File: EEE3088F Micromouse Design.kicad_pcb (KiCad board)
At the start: 2 copper layers, 70 x 78.2 mm, 47 parts, among them J1 Conn_02x16_Odd_Even, J2 Conn_01x02, J3 TYPE-C-31-M-12, SW1 SW_SPDT, U1 INA219AxD, U2 XL1509-3.3, U7 TPS61088RHLR, U9 CH224K

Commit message: Added a bunch of changes
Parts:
- removed C2, C4, C5, C6: 100uF, Capacitor_SMD:C_1206_3216Metric_Pad1.33x1.80mm_HandSolder
- removed C7: 47uF, Capacitor_SMD:C_1206_3216Metric_Pad1.33x1.80mm_HandSolder
- removed D1: 1N5819, Diode_THT:D_DO-41_SOD81_P10.16mm_Horizontal
- added C12: 100uF, Capacitor_Tantalum_SMD:CP_EIA-3528-21_Kemet-B, F.Cu at (182.1, 121.7)
- added C14: 47uF, Capacitor_SMD:C_1206_3216Metric_Pad1.33x1.80mm_HandSolder, F.Cu at (182.1, 125.0)
- added C15: 47uF, Capacitor_SMD:C_1206_3216Metric_Pad1.33x1.80mm_HandSolder, F.Cu at (182.1, 128.4)
- added C26: 100uF, Capacitor_Tantalum_SMD:CP_EIA-3528-21_Kemet-B, F.Cu at (188.8, 114.0)
- added C27: 1uF, Capacitor_SMD:C_0402_1005Metric_Pad0.74x0.62mm_HandSolder, F.Cu at (182.9, 94.7)
- added C28: 10nF, Capacitor_SMD:C_0603_1608Metric, F.Cu at (175.9, 142.8)
- added C29: 2.2uF, Capacitor_SMD:C_0603_1608Metric_Pad1.08x0.95mm_HandSolder, F.Cu at (180.0, 139.1)
- added C30: 10nF, Capacitor_SMD:C_0603_1608Metric, F.Cu at (162.0, 145.8)
- added C31: 2.2uF, Capacitor_SMD:C_0603_1608Metric_Pad1.08x0.95mm_HandSolder, F.Cu at (153.8, 136.2)
- added C32: 1uF, Capacitor_SMD:C_0402_1005Metric_Pad0.74x0.62mm_HandSolder, F.Cu at (182.9, 96.7)
- added C33: 1uF, Capacitor_SMD:C_0402_1005Metric_Pad0.74x0.62mm_HandSolder, F.Cu at (182.9, 98.7)
- added C34: 1uF, Capacitor_SMD:C_0402_1005Metric_Pad0.74x0.62mm_HandSolder, F.Cu at (182.9, 100.6)
- added C35: 1nF, Capacitor_SMD:C_0603_1608Metric, F.Cu at (179.0, 97.5)
- added C36: 1nF, Capacitor_SMD:C_0603_1608Metric, F.Cu at (179.0, 100.0)
- added C37: 100uF, Capacitor_Tantalum_SMD:CP_EIA-3528-21_Kemet-B, F.Cu at (115.8, 101.5)
- added C38: 100uF, Capacitor_Tantalum_SMD:CP_EIA-3528-21_Kemet-B, F.Cu at (115.8, 105.9)
- added C40: 100uF, Capacitor_Tantalum_SMD:CP_EIA-3528-21_Kemet-B, F.Cu at (115.8, 110.2)
- added C41: 10uF, Capacitor_SMD:C_0805_2012Metric_Pad1.18x1.45mm_HandSolder, F.Cu at (180.1, 135.8)
- added C44: 10uF, Capacitor_SMD:C_0805_2012Metric_Pad1.18x1.45mm_HandSolder, F.Cu at (185.4, 91.9)
- added C45: 10uF, Capacitor_SMD:C_0805_2012Metric_Pad1.18x1.45mm_HandSolder, F.Cu at (162.4, 143.0)
- added C46: 100uF, Capacitor_Tantalum_SMD:CP_EIA-3528-21_Kemet-B, F.Cu at (115.8, 114.6)
- added C47: 47uF, Capacitor_SMD:C_1206_3216Metric_Pad1.33x1.80mm_HandSolder, F.Cu at (121.8, 105.6)
- added C48: 100uF, Capacitor_Tantalum_SMD:CP_EIA-3528-21_Kemet-B, F.Cu at (115.8, 118.9)
- added C49: 100uF, Capacitor_Tantalum_SMD:CP_EIA-3528-21_Kemet-B, F.Cu at (115.8, 123.3)
- added C50: 100uF, Capacitor_Tantalum_SMD:CP_EIA-3528-21_Kemet-B, F.Cu at (115.8, 127.6)
- added D3: SS32, Diode_SMD:D_SMA, F.Cu at (187.6, 117.3)
- added D4: SS32, Diode_SMD:D_SMA, F.Cu at (122.8, 101.6)
- added L3: 22uH, Inductor_SMD:L_7.3x7.3_H4.5, F.Cu at (204.4, 117.4)
- added L4: 22uH, Inductor_SMD:L_7.3x7.3_H4.5, F.Cu at (204.5, 125.7)
- added L5: 22uH, Inductor_SMD:L_7.3x7.3_H4.5, F.Cu at (204.7, 134.8)
- added Q2: AO3400A, Package_TO_SOT_SMD:SOT-23, F.Cu at (181.5, 113.6)
- added R19: 10k, Resistor_SMD:R_0603_1608Metric_Pad0.98x0.95mm_HandSolder, F.Cu at (179.1, 95.0)
- added R26: 1, Resistor_SMD:R_1206_3216Metric_Pad1.30x1.75mm_HandSolder, F.Cu at (180.2, 141.6)
- added R27: 4.7k, Resistor_SMD:R_1206_3216Metric_Pad1.30x1.75mm_HandSolder, F.Cu at (188.5, 121.8)
- added R28: 330, Resistor_SMD:R_0805_2012Metric_Pad1.20x1.40mm_HandSolder, F.Cu at (181.4, 117.3)
- added R29: 0.82, Resistor_SMD:R_0603_1608Metric_Pad0.98x0.95mm_HandSolder, F.Cu at (153.8, 138.7)
- added R30: 0.82, Resistor_SMD:R_0603_1608Metric_Pad0.98x0.95mm_HandSolder, F.Cu at (153.8, 141.2)
- added R31: 0.82, Resistor_SMD:R_0603_1608Metric_Pad0.98x0.95mm_HandSolder, F.Cu at (153.8, 143.7)
- added R32: 0.82, Resistor_SMD:R_0603_1608Metric_Pad0.98x0.95mm_HandSolder, F.Cu at (153.8, 146.2)
- added R33: 2.2k, Resistor_SMD:R_0603_1608Metric_Pad0.98x0.95mm_HandSolder, F.Cu at (187.7, 124.7)
- added R34: 270, Resistor_SMD:R_0603_1608Metric_Pad0.98x0.95mm_HandSolder, F.Cu at (187.7, 127.2)
- added R35: 1, Resistor_SMD:R_1206_3216Metric_Pad1.30x1.75mm_HandSolder, F.Cu at (171.6, 143.0)
- added TP10: TestPoint, TestPoint:TestPoint_Pad_D2.0mm, F.Cu at (171.2, 106.7)
- added TP11: TestPoint, TestPoint:TestPoint_Pad_D2.0mm, F.Cu at (171.2, 110.7)
- added TP12: TestPoint, TestPoint:TestPoint_Pad_D2.0mm, F.Cu at (171.2, 114.8)
- added TP13: TestPoint, TestPoint:TestPoint_Pad_D2.0mm, F.Cu at (171.2, 118.8)
- added TP14: TestPoint, TestPoint:TestPoint_Pad_D2.0mm, F.Cu at (171.2, 122.8)
- added TP2: TestPoint, TestPoint:TestPoint_Pad_D2.0mm, F.Cu at (180.1, 146.1)
- added TP4: TestPoint, TestPoint:TestPoint_Pad_D2.0mm, F.Cu at (173.9, 145.9)
- added TP6: TestPoint, TestPoint:TestPoint_Pad_D2.0mm, F.Cu at (158.0, 143.6)
- added TP8: TestPoint, TestPoint:TestPoint_Pad_D2.0mm, F.Cu at (158.0, 147.6)
- added U11: DRV8833PW, Package_SO:TSSOP-16_4.4x5mm_P0.65mm, F.Cu at (173.4, 137.6)
- added U12: DRV8833PW, Package_SO:TSSOP-16_4.4x5mm_P0.65mm, F.Cu at (160.7, 138.2)
- added U13: AP22966DC8-7, AP22966DC8-7:IC_AP22966DC8-7, F.Cu at (167.6, 99.1)
- added U14: XL1509-5.0, Package_SO:SOIC-8_3.9x4.9mm_P1.27mm, F.Cu at (195.8, 116.4)
- added U15: TP4056-42-ESOP8, Package_SO:SOIC-8-1EP_3.9x4.9mm_P1.27mm_EP2.41x3.3mm_ThermalVias, F.Cu at (195.8, 123.0)
- C13, C23, C25: footprint Capacitor_SMD:C_1206_3216Metric_Pad1.33x1.80mm_HandSolder -> Capacitor_Tantalum_SMD:CP_EIA-3528-21_Kemet-B
- moved C20 126.1 mm to (190.6, 95.8)
- moved C21 126.1 mm to (190.6, 99.1)
- moved C22 126.1 mm to (190.6, 102.5)
- moved TP20 126.1 mm to (207.7, 105.3)
- moved U7 126.1 mm to (202.3, 106.6)
- moved C1 126.1 mm to (204.2, 102.1)
- moved C16 126.1 mm to (189.2, 108.1)
- moved C17 126.1 mm to (189.2, 110.0)
- moved C18 126.1 mm to (201.8, 111.1)
- moved C19 126.1 mm to (195.6, 110.8)
- moved C39 126.1 mm to (200.8, 101.4)
- moved L2 126.1 mm to (201.8, 97.0)
- moved R21 126.1 mm to (196.6, 107.9)
- moved R4 126.1 mm to (196.0, 95.6)
- moved R5 126.1 mm to (196.6, 104.6)
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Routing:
- net GND: track 0.00 -> 17.1 mm
- net /MOTOR1_B_OUT: track 0.00 -> 3.52 mm
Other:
- board size 70 x 78.2 mm -> 70.2 x 78.6 mm
- board text added: "200mA Motor"
- board text added: "500mA Motor"
- board text added: "Battery Charging"
- board text added: "External Load Switching"

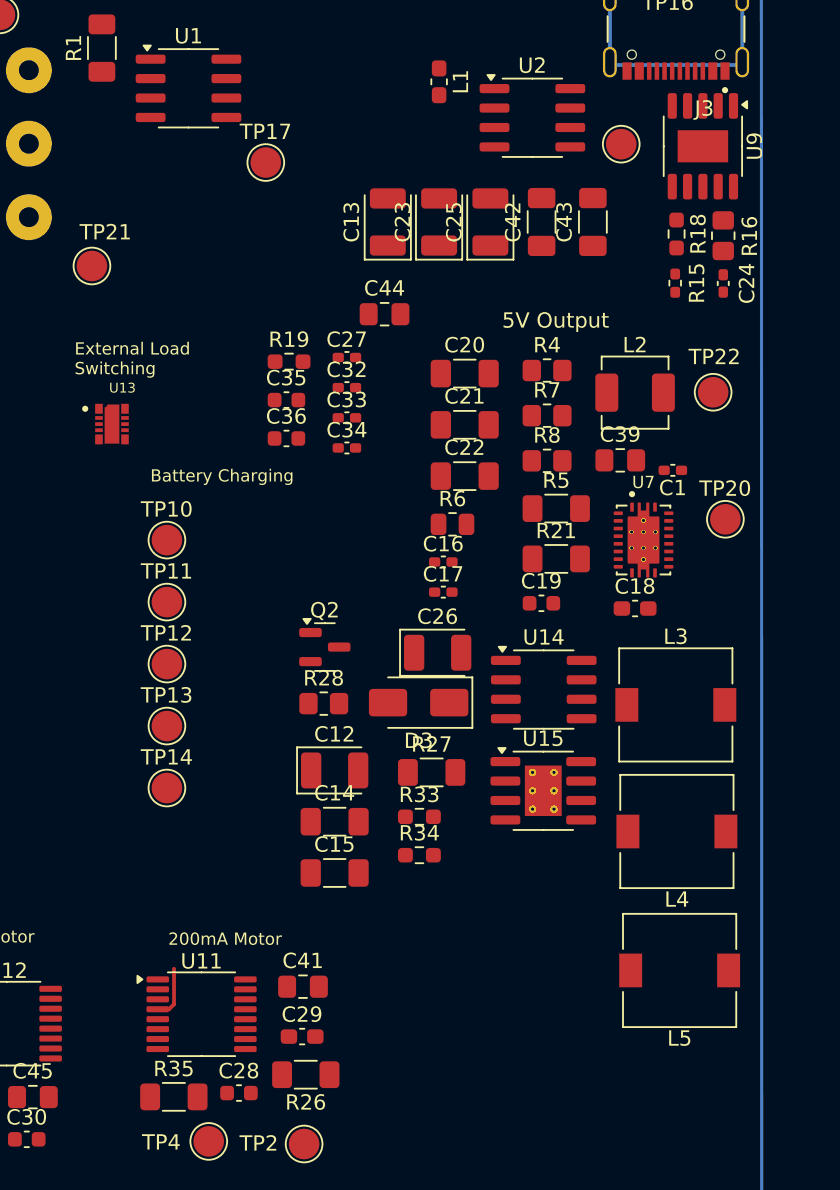
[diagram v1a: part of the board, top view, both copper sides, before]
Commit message: Updated the INA219 circuit
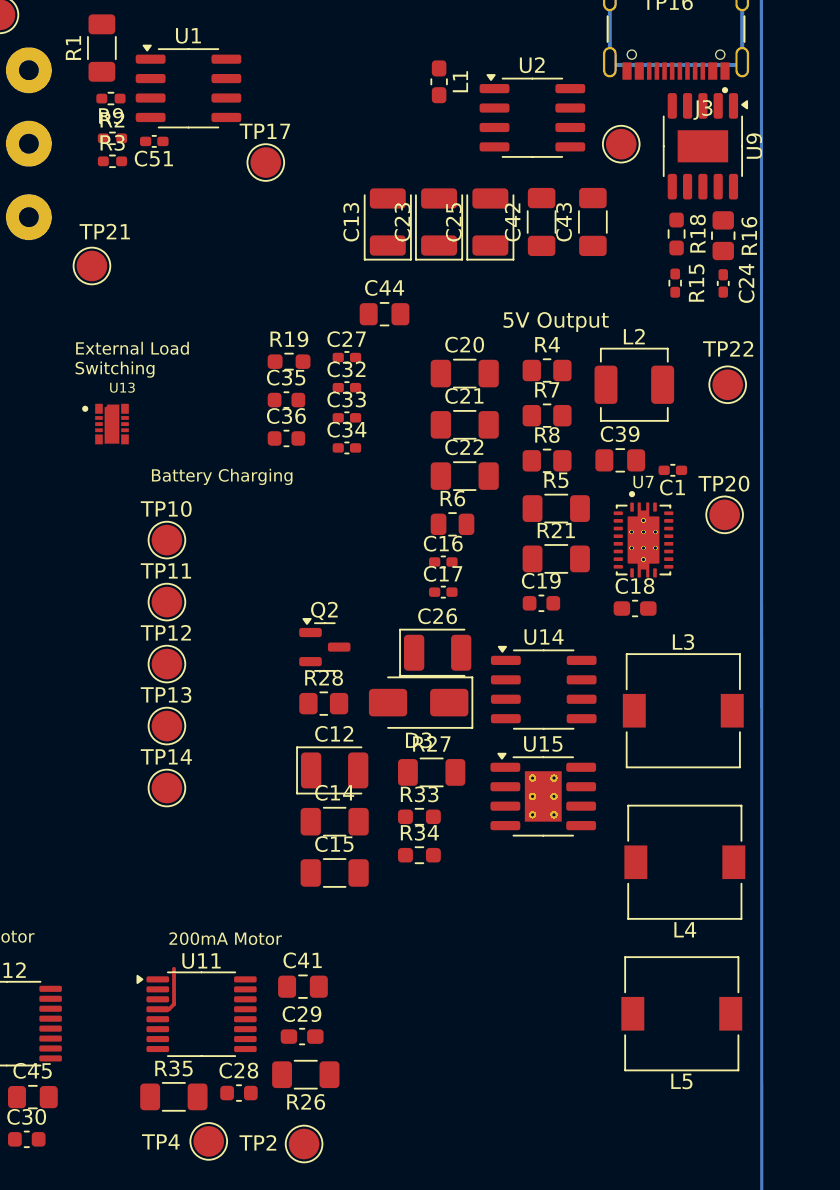
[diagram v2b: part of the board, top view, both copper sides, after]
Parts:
- added C51: 0.1uF, Capacitor_SMD:C_0402_1005Metric_Pad0.74x0.62mm_HandSolder, F.Cu at (170.3, 80.6)
- added R2: 3.3k, Resistor_SMD:R_0402_1005Metric_Pad0.72x0.64mm_HandSolder, F.Cu at (167.6, 80.4)
- added R3: 3.3k, Resistor_SMD:R_0402_1005Metric_Pad0.72x0.64mm_HandSolder, F.Cu at (167.6, 81.9)
- added R9: 3.3k, Resistor_SMD:R_0402_1005Metric_Pad0.72x0.64mm_HandSolder, F.Cu at (167.5, 77.8)
- moved L5 2.83 mm to (204.8, 137.6)
- moved L4 2.08 mm to (205.0, 127.7)
- moved TP22 1.07 mm to (207.8, 96.5)
- moved L3 0.62 mm to (204.9, 117.8)
- moved L2 0.52 mm to (201.7, 96.5)
- moved U15 0.37 mm to (195.8, 123.4)
- moved TP20 0.29 mm to (207.6, 105.0)
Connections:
- U1 pad 1: /V_Battery+ -> Net-(U1-A1)
- U1 pad 3: /SDA_INA219 -> Net-(U1-SDA)
- U1 pad 4: /SCLK_INA219 -> Net-(U1-SCL)

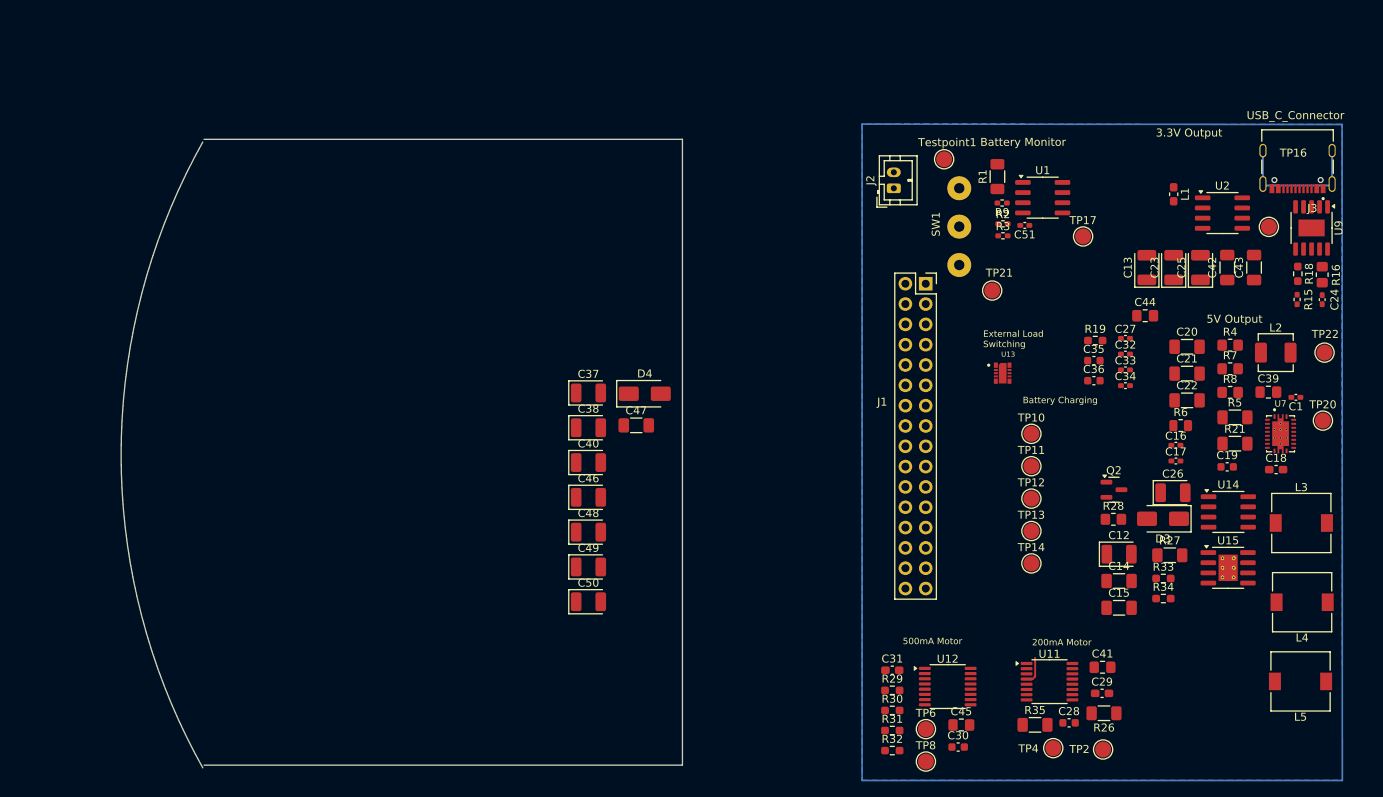
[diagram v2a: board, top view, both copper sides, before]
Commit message: First turnover, changed pcb layout
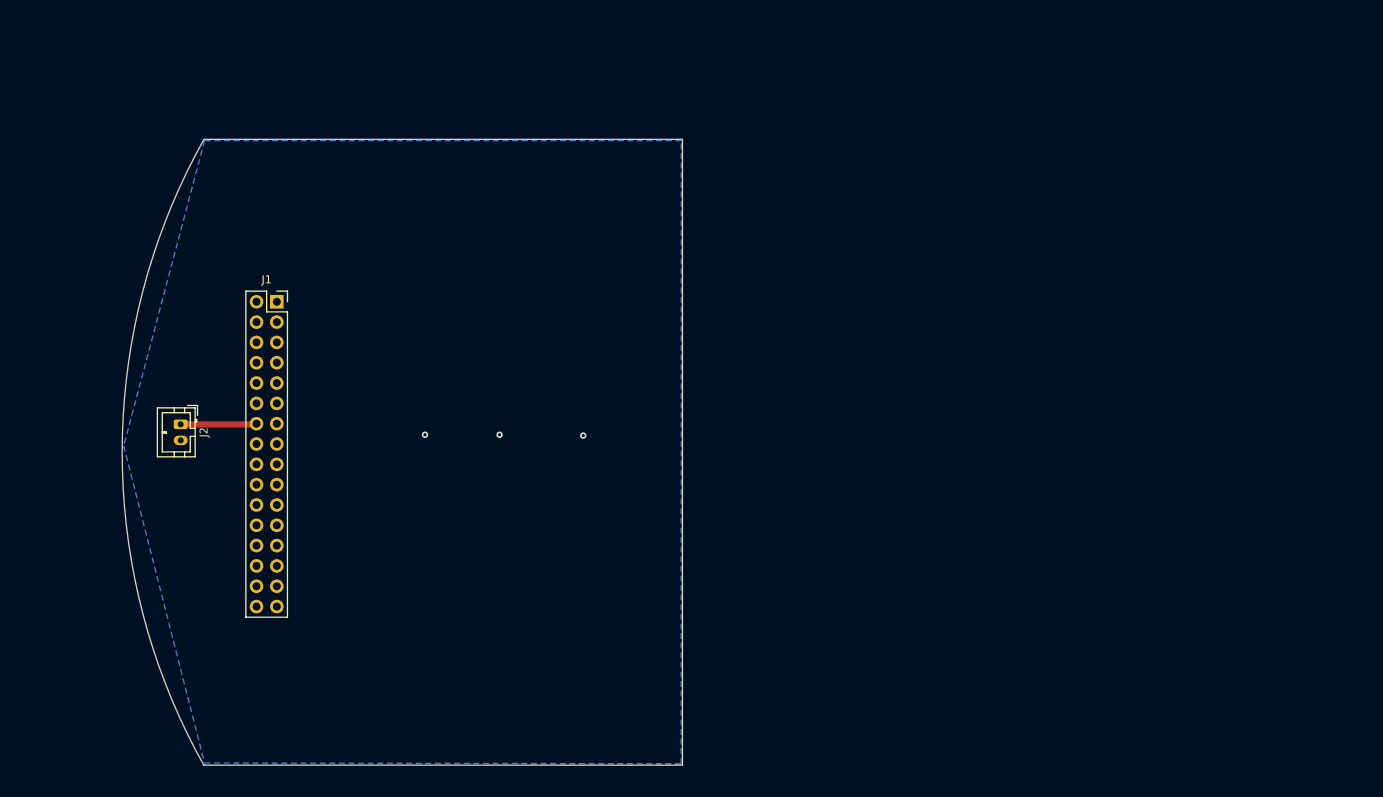
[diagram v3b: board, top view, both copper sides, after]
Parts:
- removed C1, C24, C27, C32, C33, C34: 1uF, Capacitor_SMD:C_0402_1005Metric_Pad0.74x0.62mm_HandSolder
- removed C12, C13, C23, C25, C26, C37, C38, C40, C46, C48, C49, C50: 100uF, Capacitor_Tantalum_SMD:CP_EIA-3528-21_Kemet-B
- removed C14, C15, C42, C43, C47: 47uF, Capacitor_SMD:C_1206_3216Metric_Pad1.33x1.80mm_HandSolder
- removed C16, C17, C51: 0.1uF, Capacitor_SMD:C_0402_1005Metric_Pad0.74x0.62mm_HandSolder
- removed C18: 47nF, Capacitor_SMD:C_0603_1608Metric_Pad1.08x0.95mm_HandSolder
- removed C19, C35, C36: 1nF, Capacitor_SMD:C_0603_1608Metric
- removed C20, C21, C22: 22uF, Capacitor_SMD:C_1206_3216Metric_Pad1.33x1.80mm_HandSolder
- removed C28, C30: 10nF, Capacitor_SMD:C_0603_1608Metric
- removed C29, C31: 2.2uF, Capacitor_SMD:C_0603_1608Metric_Pad1.08x0.95mm_HandSolder
- removed C39, C41, C44, C45: 10uF, Capacitor_SMD:C_0805_2012Metric_Pad1.18x1.45mm_HandSolder
- removed D3, D4: SS32, Diode_SMD:D_SMA
- removed J3: TYPE-C-31-M-12, Footprints:HRO_TYPE-C-31-M-12
- removed L1: 22uH, Inductor_SMD:L_0603_1608Metric_Pad1.05x0.95mm_HandSolder
- removed L2: 1.2uH, Inductor_SMD:L_Changjiang_FXL0420
- removed L3, L4, L5: 22uH, Inductor_SMD:L_7.3x7.3_H4.5
- removed Q2: AO3400A, Package_TO_SOT_SMD:SOT-23
- removed R1: 0.1, Resistor_SMD:R_1206_3216Metric_Pad1.30x1.75mm_HandSolder
- removed R15: 1k, Resistor_SMD:R_0402_1005Metric_Pad0.72x0.64mm_HandSolder
- removed R16: 6.8k, Resistor_SMD:R_0805_2012Metric_Pad1.20x1.40mm_HandSolder
- removed R18, R19: 10k, Resistor_SMD:R_0603_1608Metric_Pad0.98x0.95mm_HandSolder
- removed R2, R3, R9: 3.3k, Resistor_SMD:R_0402_1005Metric_Pad0.72x0.64mm_HandSolder
- removed R21: 33k, Resistor_SMD:R_1206_3216Metric_Pad1.30x1.75mm_HandSolder
- removed R26, R35: 1, Resistor_SMD:R_1206_3216Metric_Pad1.30x1.75mm_HandSolder
- removed R27: 4.7k, Resistor_SMD:R_1206_3216Metric_Pad1.30x1.75mm_HandSolder
- removed R28: 330, Resistor_SMD:R_0805_2012Metric_Pad1.20x1.40mm_HandSolder
- removed R29, R30, R31, R32: 0.82, Resistor_SMD:R_0603_1608Metric_Pad0.98x0.95mm_HandSolder
- removed R33: 2.2k, Resistor_SMD:R_0603_1608Metric_Pad0.98x0.95mm_HandSolder
- removed R34: 270, Resistor_SMD:R_0603_1608Metric_Pad0.98x0.95mm_HandSolder
- removed R4: 220k, Resistor_SMD:R_0805_2012Metric_Pad1.20x1.40mm_HandSolder
- removed R5: 100k, Resistor_SMD:R_1206_3216Metric_Pad1.30x1.75mm_HandSolder
- removed R6: 68k, Resistor_SMD:R_0805_2012Metric
- removed R7: 47k, Resistor_SMD:R_0805_2012Metric_Pad1.20x1.40mm_HandSolder
- removed R8: 150k, Resistor_SMD:R_0805_2012Metric_Pad1.20x1.40mm_HandSolder
- removed SW1: SW_SPDT, HX_SS12D10G6_Switch:Untitled
- removed TP10, TP11, TP12, TP13, TP14, TP16, TP17, TP2, TP20, TP21, TP22, TP4, TP6, TP8, Testpoint1: TestPoint, TestPoint:TestPoint_Pad_D2.0mm
- removed U1: INA219AxD, Package_SO:SOIC-8_3.9x4.9mm_P1.27mm
- removed U11, U12: DRV8833PW, Package_SO:TSSOP-16_4.4x5mm_P0.65mm
- removed U13: AP22966DC8-7, AP22966DC8-7:IC_AP22966DC8-7
- removed U14: XL1509-5.0, Package_SO:SOIC-8_3.9x4.9mm_P1.27mm
- removed U15: TP4056-42-ESOP8, Package_SO:SOIC-8-1EP_3.9x4.9mm_P1.27mm_EP2.41x3.3mm_ThermalVias
- removed U2: XL1509-3.3, Package_SO:SOIC-8_3.9x4.9mm_P1.27mm
- removed U7: TPS61088RHLR, TPS61088:IC_TPS61088RHLR
- removed U9: CH224K, Package_SO:SSOP-10-1EP_3.9x4.9mm_P1mm_EP2.1x3.3mm
- moved J2 93.9 mm to (64.8, 105.5), turned to -90 degrees
- moved J1 81.1 mm to (76.8, 90.1)
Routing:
- net GND: track 17.1 -> 0.00 mm
- net /V_Battery+: track 0.00 -> 9.51 mm
- net /MOTOR1_B_OUT: track 3.52 -> 0.00 mm
- net (no net): vias 0 -> 3
- added copper zone on B.Cu, net (none)
- removed copper zone on B.Cu, net GND
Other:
- board size 70.2 x 78.6 mm -> 70 x 78.3 mm
- board text removed: "200mA Motor"
- board text removed: "3.3V Output"
- board text removed: "500mA Motor"
- board text removed: "5V Output"
- board text removed: "Battery Charging"
- board text removed: "Battery Monitor"
- board text removed: "External Load Switching"
- board text removed: "USB_C_Connector"

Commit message: Fixing errors
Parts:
- added C51: 0.1uF, Capacitor_SMD:C_0402_1005Metric_Pad0.74x0.62mm_HandSolder, F.Cu at (89.7, 82.4)
- added R1: 0.1, Resistor_SMD:R_1206_3216Metric_Pad1.30x1.75mm_HandSolder, F.Cu at (87.0, 79.8)
- added R2: 3.3k, Resistor_SMD:R_0402_1005Metric_Pad0.72x0.64mm_HandSolder, F.Cu at (91.0, 71.3)
- added R3: 3.3k, Resistor_SMD:R_0402_1005Metric_Pad0.72x0.64mm_HandSolder, F.Cu at (91.0, 73.3)
- added R9: 3.3k, Resistor_SMD:R_0402_1005Metric_Pad0.72x0.64mm_HandSolder, F.Cu at (91.0, 75.3)
- added SW1: SW_SPDT, HX_SS12D10G6_Switch:Untitled, F.Cu at (82.5, 74.2)
- added Testpoint1: TestPoint, TestPoint:TestPoint_Pad_D2.0mm, F.Cu at (86.1, 83.4)
- added U1: INA219AxD, Package_SO:SOIC-8_3.9x4.9mm_P1.27mm, F.Cu at (79.8, 81.5)
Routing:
- net /SCLK_INA219: track 0.00 -> 57.3 mm, vias 0 -> 1
- net /5V Out: track 0.00 -> 55.2 mm
- net GND: track 0.00 -> 54.6 mm, vias 0 -> 1
- net /V_Battery+: track 9.51 -> 54.7 mm
- net /SDA_INA219: track 0.00 -> 41.5 mm
- net Net-(U1-SDA): track 0.00 -> 23.4 mm, vias 0 -> 2
- net Net-(U1-SCL): track 0.00 -> 18.6 mm, vias 0 -> 2
- net Net-(U1-A1): track 0.00 -> 18.1 mm
- net Net-(SW1-B): track 0.00 -> 9.71 mm
- net (no net): vias 3 -> 0
